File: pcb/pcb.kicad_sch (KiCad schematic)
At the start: 17 parts, among them CN1 1x3, CN10 1x2, CN2 1x8, CN3 1x8, CN4 1x8, CN5 1x4, CN6 1x2, CN7 1x2, SW1 switch_3x4, SW2 switch_3x4

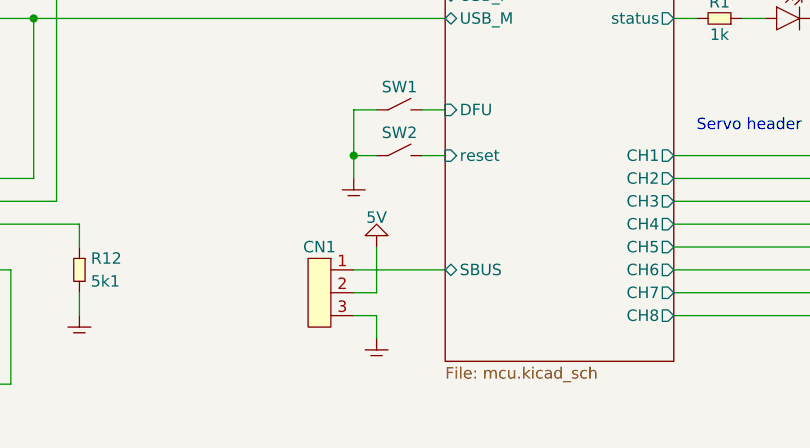
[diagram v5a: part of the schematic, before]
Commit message: removed FTDI and SBUS headers for now
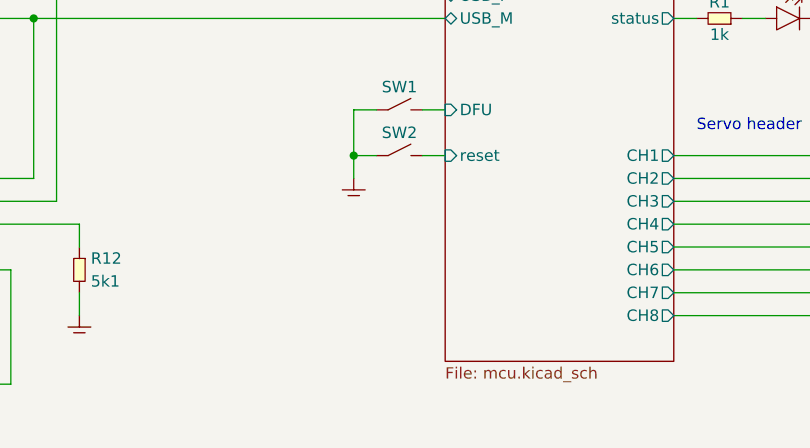
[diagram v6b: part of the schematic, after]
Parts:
- removed CN1: 1x3, symbol pin_headers:1x3
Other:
- sheet MCU ports: added none; removed SBUS
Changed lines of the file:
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@@
-    (stroke (width 0) (type default))
-  )
-  (wire (pts (xy 129.54 137.16) (xy 132.08 137.16))
     (stroke (width 0) (type default))
   )
@@
     (stroke (width 0) (type default))
   )
-  (wire (pts (xy 132.08 139.7) (xy 132.08 142.24))
-    (stroke (width 0) (type default))
-  )
   (wire (pts (xy 190.5 124.46) (xy 190.5 127))
     (stroke (width 0) (type default))
@@
     (stroke (width 0) (type default))
   )
-  (wire (pts (xy 129.54 139.7) (xy 132.08 139.7))
-    (stroke (width 0) (type default))
-  )
   (wire (pts (xy 203.2 142.24) (xy 203.2 139.7))
     (stroke (width 0) (type default))
@@
     (stroke (width 0) (type default))
   )
-  (wire (pts (xy 132.08 137.16) (xy 132.08 132.08))
-    (stroke (width 0) (type default))
-  )
   (wire (pts (xy 68.58 124.46) (xy 66.04 124.46))
     (stroke (width 0) (type default))
@@
   )
   (wire (pts (xy 93.98 124.46) (xy 93.98 106.68))
-    (stroke (width 0) (type default))
-  )
-  (wire (pts (xy 129.54 134.62) (xy 139.7 134.62))
     (stroke (width 0) (type default))
   )
@@
     )
   )
-  (symbol (lib_id "generic:GND") (at 132.08 142.24 0) (unit 1)
-    (in_bom yes) (on_board yes) (dnp no) (fields_autoplaced)
-    (property "Reference" "#GND07" (at 135.89 140.97 0)
-      (effects (font (size 1.27 1.27)) hide)
-    )
-    (property "Value" "GND" (at 135.89 142.24 0)
-      (effects (font (size 1.27 1.27)) hide)
-    )
-    (property "Footprint" "" (at 132.08 142.24 0)
-      (effects (font (size 1.27 1.27)) hide)
-    )
-    (property "Datasheet" "" (at 132.08 142.24 0)
-      (effects (font (size 1.27 1.27)) hide)
-    )
-    (pin "~")
-    (instances
-      (project "pcb"
-        (path "/6bb3bad6-1a89-4624-b34d-6ddda7dd16d2"
-          (reference "#GND07") (unit 1)
-        )
-      )
-    )
-  )
   (symbol (lib_id "switches:switch_3x4") (at 134.62 116.84 0) (unit 1)
     (in_bom yes) (on_board yes) (dnp no) (fields_autoplaced)
@@
     )
   )
-  (symbol (lib_id "pin_headers:1x3") (at 129.54 137.16 0) (mirror y) (unit 1)
-    (in_bom yes) (on_board yes) (dnp no) (fields_autoplaced)
-    (property "Reference" "CN1" (at 125.73 132.08 0)
-      (effects (font (size 1.27 1.27)))
-    )
-    (property "Value" "1x3" (at 129.54 132.08 0)
-      (effects (font (size 1.27 1.27)) hide)
-    )
-    (property "Footprint" "" (at 129.54 134.62 0)
-      (effects (font (size 1.27 1.27)) hide)
-    )
-    (property "Datasheet" "" (at 129.54 139.7 0)
-      (effects (font (size 1.27 1.27)) hide)
-    )
-    (pin "1")
-    (pin "2")
-    (pin "3")
-    (instances
-      (project "pcb"
-        (path "/6bb3bad6-1a89-4624-b34d-6ddda7dd16d2"
-          (reference "CN1") (unit 1)
-        )
-      )
-    )
-  )
-  (symbol (lib_id "generic:5V") (at 132.08 132.08 0) (unit 1)
-    (in_bom yes) (on_board yes) (dnp no)
-    (property "Reference" "#5V02" (at 135.89 130.81 0)
-      (effects (font (size 1.27 1.27)) hide)
-    )
-    (property "Value" "5V" (at 132.08 129.54 0)
-      (effects (font (size 1.27 1.27)) (justify bottom))
-    )
-    (property "Footprint" "" (at 132.08 132.08 0)
-      (effects (font (size 1.27 1.27)) hide)
-    )
-    (property "Datasheet" "" (at 132.08 132.08 0)
-      (effects (font (size 1.27 1.27)) hide)
-    )
-    (pin "~")
-    (instances
-      (project "pcb"
-        (path "/6bb3bad6-1a89-4624-b34d-6ddda7dd16d2"
-          (reference "#5V02") (unit 1)
-        )
-      )
-    )
-  )
   (symbol (lib_name "GND_1") (lib_id "generic:GND") (at 99.06 139.7 0) (unit 1)
     (in_bom yes) (on_board yes) (dnp no) (fields_autoplaced)
@@
       (effects (font (size 1.27 1.27)) (justify left))
     )
-    (pin "SBUS" bidirectional (at 139.7 134.62 180)
-      (effects (font (size 1.27 1.27)) (justify left))
-    )

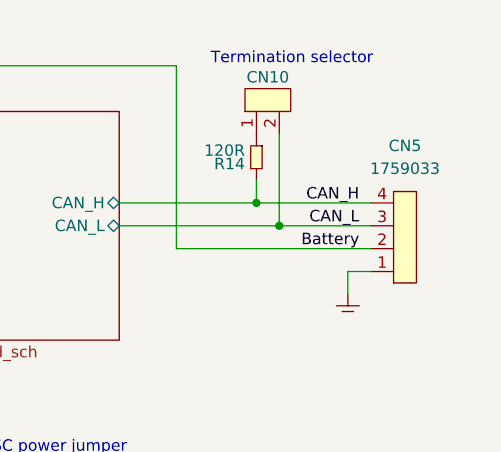
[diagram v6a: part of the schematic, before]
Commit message: added can+pwr header, worked layout
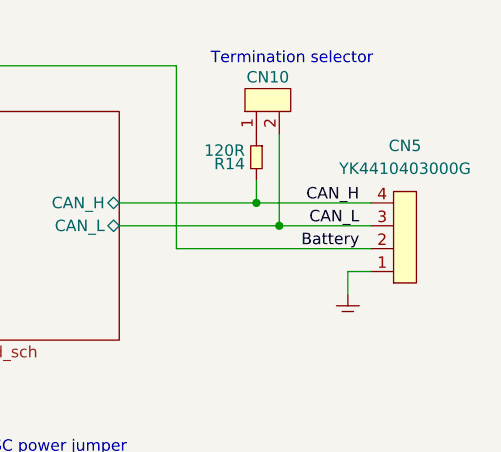
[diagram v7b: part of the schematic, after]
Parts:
- CN5: footprint (none) -> connectors:YK4410403000G; MPN 1759033 -> YK4410403000G
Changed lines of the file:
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@@
       (effects (font (size 1.27 1.27)) hide)
     )
-    (property "Footprint" "" (at 243.84 93.98 0)
+    (property "Footprint" "connectors:YK4410403000G" (at 243.84 93.98 0)
       (effects (font (size 1.27 1.27)) hide)
     )
@@
       (effects (font (size 1.27 1.27)) hide)
     )
-    (property "MPN" "1759033" (at 247.65 82.55 0)
+    (property "MPN" "YK4410403000G" (at 247.65 82.55 0)
       (effects (font (size 1.27 1.27)))
     )

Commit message: added DIP switches, footprints
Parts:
- added SW3: 219-3LPST, buttons:219-3LPST, symbol switches:219-3LPST
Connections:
- net GND: now also SW3.4, SW3.5, SW3.6
- new net MCU/ADDR1: SW3.1
- new net MCU/ADDR2: SW3.2
- new net MCU/ADDR3: SW3.3
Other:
- sheet MCU ports: added ADDR1, ADDR2, ADDR3; removed none
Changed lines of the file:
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@@
   (junction (at 190.5 137.16) (diameter 0) (color 0 0 0 0)
   )
+  (junction (at 129.54 134.62) (diameter 0) (color 0 0 0 0)
+  )
   (junction (at 76.2 147.32) (diameter 0) (color 0 0 0 0)
   )
@@
   (junction (at 203.2 132.08) (diameter 0) (color 0 0 0 0)
   )
+  (junction (at 129.54 137.16) (diameter 0) (color 0 0 0 0)
+  )
   (junction (at 73.66 147.32) (diameter 0) (color 0 0 0 0)
   )
@@
   (junction (at 93.98 106.68) (diameter 0) (color 0 0 0 0)
   )
+  (junction (at 129.54 132.08) (diameter 0) (color 0 0 0 0)
+  )
   (junction (at 78.74 147.32) (diameter 0) (color 0 0 0 0)
   )
@@
     (stroke (width 0) (type default))
   )
+  (wire (pts (xy 129.54 134.62) (xy 132.08 134.62))
+    (stroke (width 0) (type default))
+  )
   (wire (pts (xy 203.2 121.92) (xy 205.74 121.92))
     (stroke (width 0) (type default))
@@
     (stroke (width 0) (type default))
   )
+  (wire (pts (xy 129.54 132.08) (xy 129.54 121.92))
+    (stroke (width 0) (type default))
+  )
   (wire (pts (xy 203.2 137.16) (xy 205.74 137.16))
     (stroke (width 0) (type default))
@@
     (stroke (width 0) (type default))
   )
+  (wire (pts (xy 129.54 134.62) (xy 129.54 132.08))
+    (stroke (width 0) (type default))
+  )
   (wire (pts (xy 165.1 106.68) (xy 167.64 106.68))
     (stroke (width 0) (type default))
@@
     (stroke (width 0) (type default))
   )
+  (wire (pts (xy 137.16 132.08) (xy 139.7 132.08))
+    (stroke (width 0) (type default))
+  )
   (wire (pts (xy 203.2 124.46) (xy 205.74 124.46))
     (stroke (width 0) (type default))
@@
     (stroke (width 0) (type default))
   )
+  (wire (pts (xy 129.54 132.08) (xy 132.08 132.08))
+    (stroke (width 0) (type default))
+  )
   (wire (pts (xy 190.5 127) (xy 193.04 127))
     (stroke (width 0) (type default))
@@
     (stroke (width 0) (type default))
   )
+  (wire (pts (xy 137.16 137.16) (xy 139.7 137.16))
+    (stroke (width 0) (type default))
+  )
   (wire (pts (xy 190.5 124.46) (xy 190.5 127))
     (stroke (width 0) (type default))
@@
     (stroke (width 0) (type default))
   )
+  (wire (pts (xy 129.54 137.16) (xy 129.54 134.62))
+    (stroke (width 0) (type default))
+  )
+  (wire (pts (xy 129.54 137.16) (xy 132.08 137.16))
+    (stroke (width 0) (type default))
+  )
   (wire (pts (xy 129.54 121.92) (xy 132.08 121.92))
     (stroke (width 0) (type default))
@@
     (stroke (width 0) (type default))
   )
-  (wire (pts (xy 129.54 124.46) (xy 129.54 121.92))
+  (wire (pts (xy 129.54 139.7) (xy 129.54 137.16))
     (stroke (width 0) (type default))
   )
@@
   )
   (wire (pts (xy 78.74 147.32) (xy 78.74 149.86))
+    (stroke (width 0) (type default))
+  )
+  (wire (pts (xy 137.16 134.62) (xy 139.7 134.62))
     (stroke (width 0) (type default))
   )
@@
     )
   )
-  (symbol (lib_id "generic:GND") (at 129.54 124.46 0) (unit 1)
-    (in_bom yes) (on_board yes) (dnp no) (fields_autoplaced)
-    (property "Reference" "#GND01" (at 133.35 123.19 0)
-      (effects (font (size 1.27 1.27)) hide)
-    )
-    (property "Value" "GND" (at 133.35 124.46 0)
-      (effects (font (size 1.27 1.27)) hide)
-    )
-    (property "Footprint" "" (at 129.54 124.46 0)
-      (effects (font (size 1.27 1.27)) hide)
-    )
-    (property "Datasheet" "" (at 129.54 124.46 0)
+  (symbol (lib_id "generic:GND") (at 129.54 139.7 0) (unit 1)
+    (in_bom yes) (on_board yes) (dnp no) (fields_autoplaced)
+    (property "Reference" "#GND01" (at 133.35 138.43 0)
+      (effects (font (size 1.27 1.27)) hide)
+    )
+    (property "Value" "GND" (at 133.35 139.7 0)
+      (effects (font (size 1.27 1.27)) hide)
+    )
+    (property "Footprint" "" (at 129.54 139.7 0)
+      (effects (font (size 1.27 1.27)) hide)
+    )
+    (property "Datasheet" "" (at 129.54 139.7 0)
       (effects (font (size 1.27 1.27)) hide)
     )
@@
     )
   )
+  (symbol (lib_id "switches:219-3LPST") (at 134.62 132.08 0) (mirror y) (unit 1)
+    (in_bom yes) (on_board yes) (dnp no) (fields_autoplaced)
+    (property "Reference" "SW3" (at 134.62 129.54 0)
+      (effects (font (size 1.27 1.27)))
+    )
+    (property "Value" "219-3LPST" (at 134.62 125.73 0)
+      (effects (font (size 1.27 1.27)) hide)
+    )
+    (property "Footprint" "buttons:219-3LPST" (at 134.62 139.7 0)
+      (effects (font (size 1.27 1.27)) hide)
+    )
+    (property "Datasheet" "https://www.ctscorp.com/Files/DataSheets/Switches/DIP-Switches/CTS-Switches-DIP-219-Series-Datasheet.pdf" (at 135.89 124.46 0)
+      (effects (font (size 1.27 1.27)) hide)
+    )
+    (property "Digi-Key" "CT2193LPST-ND" (at 134.62 125.73 0)
+      (effects (font (size 1.27 1.27)) hide)
+    )
+    (property "MPN" "219-3LPST" (at 134.62 139.7 0)
+      (effects (font (size 1.27 1.27)) hide)
+    )
+    (pin "1")
+    (pin "2")
+    (pin "3")
+    (pin "4")
+    (pin "5")
+    (pin "6")
+    (instances
+      (project "pcb"
+        (path "/6bb3bad6-1a89-4624-b34d-6ddda7dd16d2"
+          (reference "SW3") (unit 1)
+        )
+      )
+    )
+  )
   (symbol (lib_name "GND_1") (lib_id "generic:GND") (at 58.42 139.7 0) (unit 1)
     (in_bom yes) (on_board yes) (dnp no) (fields_autoplaced)
@@
       (effects (font (size 1.27 1.27)) (justify left))
     )
+    (pin "ADDR3" input (at 139.7 137.16 180)
+      (effects (font (size 1.27 1.27)) (justify left))
+    )
+    (pin "ADDR2" input (at 139.7 134.62 180)
+      (effects (font (size 1.27 1.27)) (justify left))
+    )
+    (pin "ADDR1" input (at 139.7 132.08 180)
+      (effects (font (size 1.27 1.27)) (justify left))
+    )
